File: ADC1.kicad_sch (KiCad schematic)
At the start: 21 parts, among them U8 MCP6004

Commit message: haciendo el pcb
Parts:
- added J1: Conn_01x04_Shielded, Connector_Phoenix_SPT:PhoenixContact_SPT_2.5_4-H-5.0-EX_1x04_P5.0mm_Horizontal, symbol Connector_Generic_Shielded:Conn_01x04_Shielded
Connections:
- net AV6: no longer names the net of R58.1, RN2.4 (R4.1)
- net AV6: now also J1.1 (Pin_1)
- net AV7: no longer names the net of R56.1, RN2.3 (R3.1)
- net AV7: now also J1.2 (Pin_2)
- net AV8: no longer names the net of R54.1, RN2.2 (R2.1)
- net AV8: now also J1.3 (Pin_3)
- net AV9: no longer names the net of R52.1, R7.2, RN2.1 (R1.1)
- net AV9: now also J1.4 (Pin_4)
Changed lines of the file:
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@@
 	)
 	(junction
-		(at 191.77 66.04)
+		(at 87.63 85.09)
 		(diameter 0)
 		(color 0 0 0 0)
 	)
 	(junction
-		(at 87.63 85.09)
+		(at 68.58 87.63)
+		(diameter 0)
+		(color 0 0 0 0)
+	)
+	(junction
+		(at 191.77 66.04)
 		(diameter 0)
 		(color 0 0 0 0)
@@
 	)
 	(junction
-		(at 83.185 82.55)
+		(at 201.93 111.76)
 		(diameter 0)
 		(color 0 0 0 0)
 	)
 	(junction
-		(at 201.93 111.76)
+		(at 78.74 80.01)
 		(diameter 0)
 		(color 0 0 0 0)
 	)
 	(junction
-		(at 78.74 80.01)
+		(at 83.185 82.55)
 		(diameter 0)
 		(color 0 0 0 0)
@@
 	(wire
 		(pts
-			(xy 201.93 130.81) (xy 201.93 132.08)
+			(xy 68.58 85.09) (xy 87.63 85.09)
 		)
 		(stroke
@@
 	(wire
 		(pts
-			(xy 162.56 114.3) (xy 162.56 85.09)
-		)
-		(stroke
-			(width 0)
-			(type default)
-		)
-	)
-	(wire
-		(pts
-			(xy 142.24 109.855) (xy 142.24 80.01)
+			(xy 201.93 130.81) (xy 201.93 132.08)
 		)
 		(stroke
@@
 	(wire
 		(pts
-			(xy 64.77 87.63) (xy 92.075 87.63)
+			(xy 162.56 114.3) (xy 162.56 85.09)
 		)
 		(stroke
@@
 	(wire
 		(pts
-			(xy 83.185 82.55) (xy 104.14 82.55)
+			(xy 142.24 109.855) (xy 142.24 80.01)
 		)
 		(stroke
@@
 	(wire
 		(pts
-			(xy 92.075 87.63) (xy 104.14 87.63)
+			(xy 68.58 87.63) (xy 92.075 87.63)
 		)
 		(stroke
@@
 	(wire
 		(pts
-			(xy 64.77 80.01) (xy 78.74 80.01)
+			(xy 125.73 87.63) (xy 165.1 87.63)
 		)
 		(stroke
@@
 	(wire
 		(pts
-			(xy 87.63 93.345) (xy 87.63 85.09)
+			(xy 83.185 93.345) (xy 83.185 82.55)
 		)
 		(stroke
@@
 	(wire
 		(pts
-			(xy 125.73 87.63) (xy 165.1 87.63)
+			(xy 123.825 85.09) (xy 162.56 85.09)
 		)
 		(stroke
@@
 	(wire
 		(pts
-			(xy 83.185 93.345) (xy 83.185 82.55)
+			(xy 139.065 109.855) (xy 142.24 109.855)
 		)
 		(stroke
@@
 		)
 	)
-	(wire
+	(polyline
 		(pts
-			(xy 123.825 85.09) (xy 162.56 85.09)
+			(xy 74.93 82.55) (xy 75.565 82.55)
 		)
 		(stroke
 			(width 0)
-			(type default)
+			(type dash)
 		)
 	)
 	(wire
 		(pts
-			(xy 139.065 109.855) (xy 142.24 109.855)
+			(xy 78.74 68.58) (xy 78.74 70.485)
 		)
 		(stroke
@@
 		)
 	)
-	(polyline
+	(wire
 		(pts
-			(xy 74.93 82.55) (xy 75.565 82.55)
+			(xy 83.185 82.55) (xy 104.14 82.55)
 		)
 		(stroke
 			(width 0)
-			(type dash)
+			(type default)
 		)
 	)
 	(wire
 		(pts
-			(xy 78.74 68.58) (xy 78.74 70.485)
+			(xy 114.3 85.09) (xy 123.825 85.09)
 		)
 		(stroke
@@
 	(wire
 		(pts
-			(xy 114.3 85.09) (xy 123.825 85.09)
+			(xy 157.48 80.01) (xy 168.91 80.01)
 		)
 		(stroke
@@
 	(wire
 		(pts
-			(xy 157.48 80.01) (xy 168.91 80.01)
+			(xy 127 112.395) (xy 128.905 112.395)
 		)
 		(stroke
@@
 	(wire
 		(pts
-			(xy 127 112.395) (xy 128.905 112.395)
+			(xy 92.075 87.63) (xy 104.14 87.63)
 		)
 		(stroke
@@
 	(wire
 		(pts
+			(xy 68.58 82.55) (xy 83.185 82.55)
+		)
+		(stroke
+			(width 0)
+			(type default)
+		)
+	)
+	(wire
+		(pts
 			(xy 198.12 74.295) (xy 199.39 74.295)
 		)
@@
 	(wire
 		(pts
-			(xy 78.74 93.345) (xy 78.74 80.01)
+			(xy 78.74 80.01) (xy 78.74 93.345)
 		)
 		(stroke
@@
 		)
 	)
-	(wire
+	(polyline
 		(pts
-			(xy 64.77 82.55) (xy 83.185 82.55)
+			(xy 207.01 86.36) (xy 199.39 86.36)
 		)
 		(stroke
 			(width 0)
-			(type default)
+			(type dash)
 		)
 	)
 	(wire
 		(pts
-			(xy 64.77 85.09) (xy 87.63 85.09)
+			(xy 87.63 85.09) (xy 87.63 93.345)
 		)
 		(stroke
@@
 		)
 	)
-	(polyline
+	(wire
 		(pts
-			(xy 207.01 86.36) (xy 199.39 86.36)
+			(xy 217.17 87.63) (xy 219.71 87.63)
 		)
 		(stroke
 			(width 0)
-			(type dash)
+			(type default)
 		)
 	)
 	(wire
 		(pts
-			(xy 217.17 87.63) (xy 219.71 87.63)
+			(xy 144.145 114.935) (xy 144.145 82.55)
 		)
 		(stroke
@@
 	(wire
 		(pts
-			(xy 144.145 114.935) (xy 144.145 82.55)
+			(xy 78.74 80.01) (xy 104.14 80.01)
 		)
 		(stroke
@@
 	(wire
 		(pts
-			(xy 78.74 80.01) (xy 104.14 80.01)
+			(xy 176.53 76.2) (xy 172.72 76.2)
 		)
 		(stroke
@@
 	(wire
 		(pts
-			(xy 176.53 76.2) (xy 172.72 76.2)
+			(xy 68.58 88.9) (xy 68.58 87.63)
 		)
 		(stroke
@@
 	(wire
 		(pts
+			(xy 68.58 80.01) (xy 78.74 80.01)
+		)
+		(stroke
+			(width 0)
+			(type default)
+		)
+	)
+	(wire
+		(pts
 			(xy 191.77 104.14) (xy 198.12 104.14)
 		)
@@
 		)
 	)
-	(hierarchical_label "AV8"
-		(shape input)
-		(at 64.77 82.55 180)
-		(effects
-			(font
-				(size 1.524 1.524)
-				(thickness 0.3048)
-				(bold yes)
-			)
-			(justify right)
-		)
-	)
-	(hierarchical_label "AV6"
-		(shape input)
-		(at 64.77 87.63 180)
-		(effects
-			(font
-				(size 1.524 1.524)
-				(thickness 0.3048)
-				(bold yes)
-			)
-			(justify right)
-		)
-	)
 	(hierarchical_label "AV6_MCU"
 		(shape input)
@@
 		)
 	)
-	(hierarchical_label "AV9"
-		(shape input)
-		(at 64.77 80.01 180)
-		(effects
-			(font
-				(size 1.524 1.524)
-				(thickness 0.3048)
-				(bold yes)
-			)
-			(justify right)
-		)
-	)
 	(hierarchical_label "AV8_MCU"
 		(shape input)
@@
 		)
 	)
-	(hierarchical_label "AV7"
-		(shape input)
-		(at 64.77 85.09 180)
-		(effects
-			(font
-				(size 1.524 1.524)
-				(thickness 0.3048)
-				(bold yes)
-			)
-			(justify right)
-		)
-	)
 	(symbol
 		(lib_id "Device:C")
@@
 					(unit 1)
 				)
+			)
+		)
+	)
+	(symbol
+		(lib_id "Connector_Generic_Shielded:Conn_01x04_Shielded")
+		(at 63.5 85.09 180)
+		(unit 1)
+		(body_style 1)
+		(exclude_from_sim no)
+		(in_bom yes)
+		(on_board yes)
+		(in_pos_files yes)
+		(dnp no)
+		(fields_autoplaced yes)
+		(property "Reference" "J1"
+			(at 60.96 82.5499 0)
+			(show_name no)
+			(do_not_autoplace no)
+			(effects
+				(font
+					(size 1.27 1.27)
+				)
+				(justify left)
+			)
+		)
+		(property "Value" "Conn_01x04_Shielded"
+			(at 60.96 85.0899 0)
+			(show_name no)
+			(do_not_autoplace no)
+			(effects
+				(font
+					(size 1.27 1.27)
+				)
+				(justify left)
+			)
+		)
+		(property "Footprint" "Connector_Phoenix_SPT:PhoenixContact_SPT_2.5_4-H-5.0-EX_1x04_P5.0mm_Horizontal"
+			(at 63.5 85.09 0)
+			(hide yes)
+			(show_name no)
+			(do_not_autoplace no)
+			(effects
+				(font
+					(size 1.27 1.27)
+				)
+			)
+		)
+		(property "Datasheet" ""
+			(at 63.5 85.09 0)
+			(hide yes)
+			(show_name no)
+			(do_not_autoplace no)
+			(effects
+				(font
+					(size 1.27 1.27)
+				)
+			)
+		)
+		(property "Description" "Generic shielded connector, single row, 01x04, script generated (kicad-library-utils/schlib/autogen/connector/)"
+			(at 63.5 85.09 0)
+			(hide yes)
+			(show_name no)
+			(do_not_autoplace no)
+			(effects
+				(font
+					(size 1.27 1.27)
+				)
+			)
+		)
+		(pin "SH"
+		)
+		(pin "4"
+		)
+		(pin "1"
+		)
+		(pin "2"
+		)
+		(pin "3"
+		)
+		(instances
+			(project "ADC1"
+				(path "/2a1381e6-d7f3-4ca8-8ebb-da5f70281df7"
+					(reference "J1")
+					(unit 1)
+				)

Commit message: seguimos trabajando
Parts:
- J1: footprint Connector_Phoenix_SPT:PhoenixContact_SPT_2.5_4-H-5.0-EX_1x04_P5.0mm_Horizontal -> TerminalBlock_Phoenix:TerminalBlock_Phoenix_MKDS-1,5-4-5.08_1x04_P5.08mm_Horizontal
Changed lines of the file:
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@@
 			)
 		)
-		(property "Footprint" "Connector_Phoenix_SPT:PhoenixContact_SPT_2.5_4-H-5.0-EX_1x04_P5.0mm_Horizontal"
+		(property "Footprint" "TerminalBlock_Phoenix:TerminalBlock_Phoenix_MKDS-1,5-4-5.08_1x04_P5.08mm_Horizontal"
 			(at 63.5 85.09 0)
 			(hide yes)

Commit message: seguimos con el PCB
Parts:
- added J2: Screw_Terminal_01x04, TerminalBlock_Phoenix:TerminalBlock_Phoenix_MKDS-1,5-4-5.08_1x04_P5.08mm_Horizontal, symbol Connector:Screw_Terminal_01x04
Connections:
- net AV6_MCU: no longer names the net of R59.1, R63.2
- net AV6_MCU: now also J2.1 (Pin_1)
- net AV7_MCU: no longer names the net of R57.1, R62.2
- net AV7_MCU: now also J2.2 (Pin_2)
- net AV8_MCU: no longer names the net of R55.1, R61.2
- net AV8_MCU: now also J2.3 (Pin_3)
- net AV9_MCU: no longer names the net of R53.1, R60.2
- net AV9_MCU: now also J2.4 (Pin_4)
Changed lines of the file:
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@@
 	(wire
 		(pts
+			(xy 209.55 74.295) (xy 209.55 95.25)
+		)
+		(stroke
+			(width 0)
+			(type default)
+		)
+	)
+	(wire
+		(pts
 			(xy 168.91 101.6) (xy 176.53 101.6)
 		)
@@
 	(wire
 		(pts
+			(xy 214.63 83.185) (xy 214.63 95.25)
+		)
+		(stroke
+			(width 0)
+			(type default)
+		)
+	)
+	(wire
+		(pts
 			(xy 227.33 78.74) (xy 227.33 83.185)
 		)
@@
 	(wire
 		(pts
-			(xy 217.17 90.805) (xy 217.17 87.63)
+			(xy 217.17 87.63) (xy 217.17 95.25)
 		)
 		(stroke
@@
 	(wire
 		(pts
-			(xy 209.55 90.805) (xy 209.55 74.295)
-		)
-		(stroke
-			(width 0)
-			(type default)
-		)
-	)
-	(wire
-		(pts
-			(xy 214.63 90.805) (xy 214.63 83.185)
-		)
-		(stroke
-			(width 0)
-			(type default)
-		)
-	)
-	(wire
-		(pts
 			(xy 139.065 114.935) (xy 144.145 114.935)
 		)
@@
 	(wire
 		(pts
-			(xy 212.09 90.805) (xy 212.09 78.74)
+			(xy 212.09 78.74) (xy 212.09 95.25)
 		)
 		(stroke
@@
 		)
 	)
-	(hierarchical_label "AV6_MCU"
-		(shape input)
-		(at 217.17 90.805 270)
-		(effects
-			(font
-				(size 1.524 1.524)
-				(thickness 0.3048)
-				(bold yes)
-			)
-			(justify right)
-		)
-	)
 	(hierarchical_label "5V"
 		(shape input)
@@
 		)
 	)
-	(hierarchical_label "AV8_MCU"
-		(shape input)
-		(at 212.09 90.805 270)
-		(effects
-			(font
-				(size 1.524 1.524)
-				(thickness 0.3048)
-				(bold yes)
-			)
-			(justify right)
-		)
-	)
-	(hierarchical_label "AV9_MCU"
-		(shape input)
-		(at 209.55 90.805 270)
-		(effects
-			(font
-				(size 1.524 1.524)
-				(thickness 0.3048)
-				(bold yes)
-			)
-			(justify right)
-		)
-	)
-	(hierarchical_label "AV7_MCU"
-		(shape input)
-		(at 214.63 90.805 270)
-		(effects
-			(font
-				(size 1.524 1.524)
-				(thickness 0.3048)
-				(bold yes)
-			)
-			(justify right)
-		)
-	)
 	(hierarchical_label "AGND"
 		(shape input)
@@
 					(unit 1)
 				)
+			)
+		)
+	)
+	(symbol
+		(lib_id "Connector:Screw_Terminal_01x04")
+		(at 214.63 100.33 270)
+		(unit 1)
+		(body_style 1)
+		(exclude_from_sim no)
+		(in_bom yes)
+		(on_board yes)
+		(in_pos_files yes)
+		(dnp no)
+		(fields_autoplaced yes)
+		(property "Reference" "J2"
+			(at 213.36 104.14 90)
+			(show_name no)
+			(do_not_autoplace no)
+			(effects
+				(font
+					(size 1.27 1.27)
+				)
+			)
+		)
+		(property "Value" "Screw_Terminal_01x04"
+			(at 213.36 106.68 90)
+			(show_name no)
+			(do_not_autoplace no)
+			(effects
+				(font
+					(size 1.27 1.27)
+				)
+			)
+		)
+		(property "Footprint" "TerminalBlock_Phoenix:TerminalBlock_Phoenix_MKDS-1,5-4-5.08_1x04_P5.08mm_Horizontal"
+			(at 214.63 100.33 0)
+			(hide yes)
+			(show_name no)
+			(do_not_autoplace no)
+			(effects
+				(font
+					(size 1.27 1.27)
+				)
+			)
+		)
+		(property "Datasheet" ""
+			(at 214.63 100.33 0)
+			(hide yes)
+			(show_name no)
+			(do_not_autoplace no)
+			(effects
+				(font
+					(size 1.27 1.27)
+				)
+			)
+		)
+		(property "Description" "Generic screw terminal, single row, 01x04, script generated (kicad-library-utils/schlib/autogen/connector/)"
+			(at 214.63 100.33 0)
+			(hide yes)
+			(show_name no)
+			(do_not_autoplace no)
+			(effects
+				(font
+					(size 1.27 1.27)
+				)
+			)
+		)
+		(pin "3"
+		)
+		(pin "4"
+		)
+		(pin "2"
+		)
+		(pin "1"
+		)
+		(instances
+			(project "ADC1"
+				(path "/2a1381e6-d7f3-4ca8-8ebb-da5f70281df7"
+					(reference "J2")
+					(unit 1)
+				)

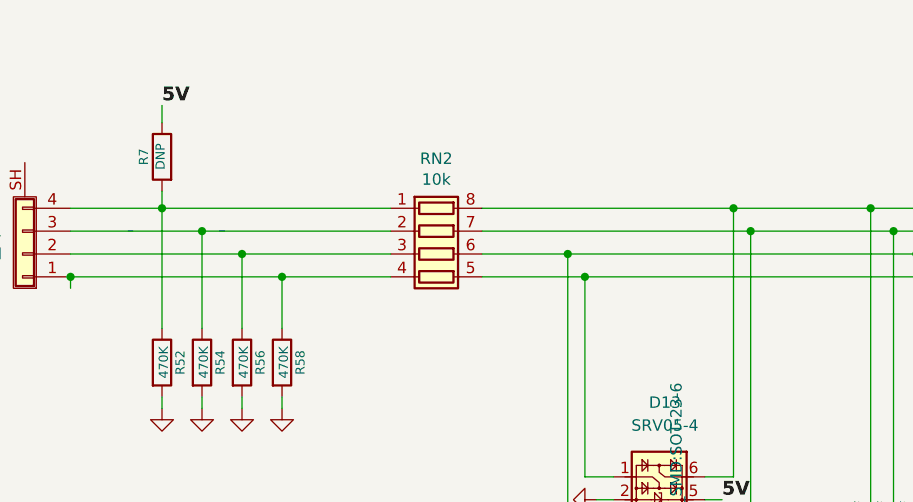
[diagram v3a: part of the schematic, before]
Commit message: cambio conjunto de resistencias de entrada
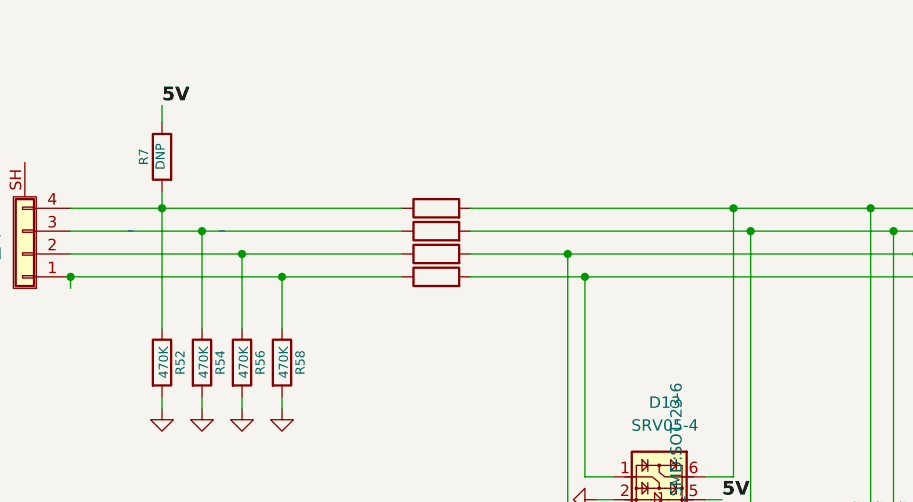
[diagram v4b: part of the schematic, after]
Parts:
- removed RN2: 10k, Resistor_SMD:R_Array_Convex_4x0603, symbol Device:R_Pack04
- added R1, R2, R3, R4: 10k, Resistor_SMD:R_0603_1608Metric, symbol Device:R
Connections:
- net at C46.1, D13.3, U8.12 (+): now also R3.2
- net at C47.1, D13.1, U8.10 (+): now also R4.2
- net at C16.1, D13.6, U8.5 (+): now also R1.2
- net at C45.1, D13.4, U8.3 (+): now also R2.2
- net at J1.2 (Pin_2), R56.1: now also R3.1
- net at J1.3 (Pin_3), R54.1: now also R2.1
- net at J1.4 (Pin_4), R52.1, R7.2: now also R1.1
- net at J1.1 (Pin_1), R58.1: now also R4.1
